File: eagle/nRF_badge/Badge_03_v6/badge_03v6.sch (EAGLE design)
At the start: 43 parts, among them J1 PROG_CONN_6, U1 LIS2DH12, U2 LP2985LV, U3 MCP6231, U5 M95M02, Y1 32768Hz

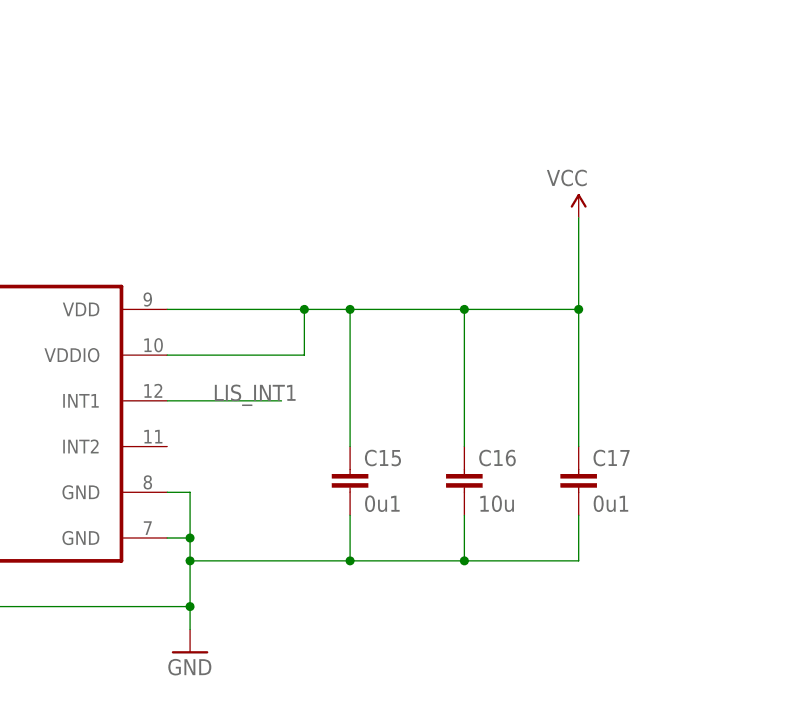
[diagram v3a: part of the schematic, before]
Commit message: Traces cleanup
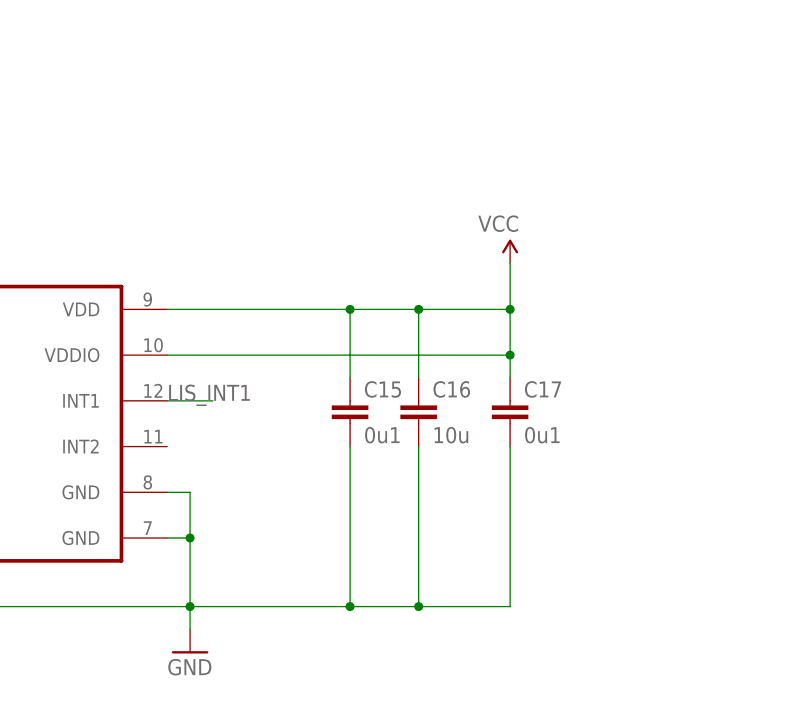
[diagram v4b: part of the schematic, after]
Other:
- moved on the sheet: C15, C16, C17
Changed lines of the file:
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@@
 <instance part="SUPPLY15" gate="G$1" x="12.7" y="43.18" rot="MR0"/>
 <instance part="GND9" gate="1" x="200.66" y="-40.64"/>
-<instance part="C15" gate="G$1" x="218.44" y="-20.32"/>
-<instance part="C16" gate="G$1" x="231.14" y="-20.32"/>
-<instance part="C17" gate="G$1" x="243.84" y="-20.32"/>
-<instance part="SUPPLY18" gate="G$1" x="243.84" y="7.62" rot="MR0"/>
+<instance part="C15" gate="G$1" x="218.44" y="-12.7"/>
+<instance part="C16" gate="G$1" x="226.06" y="-12.7"/>
+<instance part="C17" gate="G$1" x="236.22" y="-12.7"/>
+<instance part="SUPPLY18" gate="G$1" x="236.22" y="2.54" rot="MR0"/>
 <instance part="U1" gate="G$1" x="177.8" y="-15.24"/>
 </instances>
@@
 <wire x1="198.12" y1="-22.86" x2="200.66" y2="-22.86" width="0.1524" layer="91"/>
 <wire x1="200.66" y1="-22.86" x2="200.66" y2="-27.94" width="0.1524" layer="91"/>
-<wire x1="200.66" y1="-27.94" x2="200.66" y2="-30.48" width="0.1524" layer="91"/>
-<wire x1="200.66" y1="-30.48" x2="200.66" y2="-35.56" width="0.1524" layer="91"/>
+<wire x1="200.66" y1="-27.94" x2="200.66" y2="-35.56" width="0.1524" layer="91"/>
 <wire x1="200.66" y1="-35.56" x2="200.66" y2="-38.1" width="0.1524" layer="91"/>
 <wire x1="198.12" y1="-27.94" x2="200.66" y2="-27.94" width="0.1524" layer="91"/>
@@
 <wire x1="157.48" y1="-22.86" x2="154.94" y2="-22.86" width="0.1524" layer="91"/>
 <wire x1="154.94" y1="-22.86" x2="154.94" y2="-27.94" width="0.1524" layer="91"/>
-<pinref part="C17" gate="G$1" pin="2"/>
-<wire x1="243.84" y1="-25.4" x2="243.84" y2="-30.48" width="0.1524" layer="91"/>
-<wire x1="243.84" y1="-30.48" x2="231.14" y2="-30.48" width="0.1524" layer="91"/>
-<pinref part="C16" gate="G$1" pin="2"/>
-<wire x1="231.14" y1="-30.48" x2="218.44" y2="-30.48" width="0.1524" layer="91"/>
-<wire x1="231.14" y1="-25.4" x2="231.14" y2="-30.48" width="0.1524" layer="91"/>
-<junction x="231.14" y="-30.48"/>
-<pinref part="C15" gate="G$1" pin="2"/>
-<wire x1="218.44" y1="-25.4" x2="218.44" y2="-30.48" width="0.1524" layer="91"/>
-<junction x="218.44" y="-30.48"/>
-<wire x1="218.44" y1="-30.48" x2="200.66" y2="-30.48" width="0.1524" layer="91"/>
-<junction x="200.66" y="-30.48"/>
 <pinref part="U1" gate="G$1" pin="RES"/>
 <pinref part="U1" gate="G$1" pin="GND@6"/>
 <pinref part="U1" gate="G$1" pin="GND@7"/>
 <pinref part="U1" gate="G$1" pin="GND@8"/>
+<wire x1="200.66" y1="-35.56" x2="218.44" y2="-35.56" width="0.1524" layer="91"/>
+<pinref part="C17" gate="G$1" pin="2"/>
+<wire x1="218.44" y1="-35.56" x2="226.06" y2="-35.56" width="0.1524" layer="91"/>
+<wire x1="226.06" y1="-35.56" x2="236.22" y2="-35.56" width="0.1524" layer="91"/>
+<wire x1="236.22" y1="-35.56" x2="236.22" y2="-17.78" width="0.1524" layer="91"/>
+<pinref part="C16" gate="G$1" pin="2"/>
+<wire x1="226.06" y1="-17.78" x2="226.06" y2="-35.56" width="0.1524" layer="91"/>
+<junction x="226.06" y="-35.56"/>
+<pinref part="C15" gate="G$1" pin="2"/>
+<wire x1="218.44" y1="-17.78" x2="218.44" y2="-35.56" width="0.1524" layer="91"/>
+<junction x="218.44" y="-35.56"/>
 </segment>
 </net>
@@
 </segment>
 <segment>
-<wire x1="198.12" y1="-7.62" x2="213.36" y2="-7.62" width="0.1524" layer="91"/>
-<wire x1="198.12" y1="-2.54" x2="213.36" y2="-2.54" width="0.1524" layer="91"/>
+<pinref part="SUPPLY18" gate="G$1" pin="VCC"/>
+<pinref part="C17" gate="G$1" pin="1"/>
+<wire x1="236.22" y1="2.54" x2="236.22" y2="-2.54" width="0.1524" layer="91"/>
+<pinref part="U1" gate="G$1" pin="VDDIO"/>
+<wire x1="236.22" y1="-2.54" x2="236.22" y2="-7.62" width="0.1524" layer="91"/>
+<wire x1="236.22" y1="-7.62" x2="236.22" y2="-10.16" width="0.1524" layer="91"/>
+<wire x1="198.12" y1="-7.62" x2="236.22" y2="-7.62" width="0.1524" layer="91"/>
+<junction x="236.22" y="-7.62"/>
+<wire x1="198.12" y1="-2.54" x2="218.44" y2="-2.54" width="0.1524" layer="91"/>
+<pinref part="U1" gate="G$1" pin="VDD"/>
+<wire x1="218.44" y1="-2.54" x2="226.06" y2="-2.54" width="0.1524" layer="91"/>
 <pinref part="C15" gate="G$1" pin="1"/>
-<wire x1="213.36" y1="-2.54" x2="218.44" y2="-2.54" width="0.1524" layer="91"/>
-<wire x1="218.44" y1="-2.54" x2="218.44" y2="-17.78" width="0.1524" layer="91"/>
+<wire x1="218.44" y1="-10.16" x2="218.44" y2="-2.54" width="0.1524" layer="91"/>
+<junction x="218.44" y="-2.54"/>
 <pinref part="C16" gate="G$1" pin="1"/>
-<wire x1="231.14" y1="-17.78" x2="231.14" y2="-2.54" width="0.1524" layer="91"/>
-<wire x1="231.14" y1="-2.54" x2="218.44" y2="-2.54" width="0.1524" layer="91"/>
-<junction x="218.44" y="-2.54"/>
-<wire x1="213.36" y1="-7.62" x2="213.36" y2="-2.54" width="0.1524" layer="91"/>
-<junction x="213.36" y="-2.54"/>
-<wire x1="231.14" y1="-2.54" x2="243.84" y2="-2.54" width="0.1524" layer="91"/>
-<junction x="231.14" y="-2.54"/>
-<pinref part="C17" gate="G$1" pin="1"/>
-<wire x1="243.84" y1="-2.54" x2="243.84" y2="-17.78" width="0.1524" layer="91"/>
-<junction x="243.84" y="-2.54"/>
-<pinref part="SUPPLY18" gate="G$1" pin="VCC"/>
-<wire x1="243.84" y1="7.62" x2="243.84" y2="-2.54" width="0.1524" layer="91"/>
-<pinref part="U1" gate="G$1" pin="VDD"/>
-<pinref part="U1" gate="G$1" pin="VDDIO"/>
+<wire x1="226.06" y1="-10.16" x2="226.06" y2="-2.54" width="0.1524" layer="91"/>
+<junction x="226.06" y="-2.54"/>
+<wire x1="226.06" y1="-2.54" x2="236.22" y2="-2.54" width="0.1524" layer="91"/>
+<junction x="236.22" y="-2.54"/>
 </segment>
 </net>
@@
 <net name="LIS_INT1" class="0">
 <segment>
-<wire x1="198.12" y1="-12.7" x2="210.82" y2="-12.7" width="0.1524" layer="91"/>
+<wire x1="198.12" y1="-12.7" x2="203.2" y2="-12.7" width="0.1524" layer="91"/>
 <pinref part="U1" gate="G$1" pin="INT1"/>
-<label x="203.2" y="-12.7" size="1.778" layer="95"/>
-</segment>
-<segment>
+<label x="198.12" y="-12.7" size="1.778" layer="95"/>
+</segment>
+<segment>

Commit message: change component for comliant design with technical note TN0018
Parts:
- U1: device Badge:LIS2DH12 -> st-microelectronics_modified:LIS2DH12

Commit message: Fix for issues generated in last commit, updated library
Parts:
- U1: value LIS2DH12 -> LIS2DH12"; device st-microelectronics_modified:LIS2DH12 -> Badge:LIS2DH12"
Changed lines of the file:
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@@
 <part name="C17" library="rcl" library_urn="urn:adsk.eagle:library:334" deviceset="C-EU" device="C0603" package3d_urn="urn:adsk.eagle:package:23616/2" value="0u1"/>
 <part name="SUPPLY18" library="Badge" deviceset="VCC" device=""/>
-<part name="U1" library="st-microelectronics_modified" deviceset="LIS2DH12" device=""/>
+<part name="U1" library="Badge" deviceset="LIS2DH12" device="&quot;"/>
 </parts>
 <sheets>

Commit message: Approved Overlap in jumpar pad, errors is cause by DRC but package is fine.
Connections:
- net N$6 renamed ON/OFF
- net N$9 renamed BYPASS
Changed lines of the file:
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@@
 <part name="C4" library="rcl" library_urn="urn:adsk.eagle:library:334" deviceset="C-EU" device="C0603" package3d_urn="urn:adsk.eagle:package:23616/2" value="12p"/>
 <part name="GND10" library="Badge" deviceset="GND" device=""/>
-<part name="M_ENA" library="Badge" deviceset="JUMPER-PAD-3-2OF3_NC_BY_TRACE" device="_SMALL" value=""/>
+<part name="M_ENA" library="Badge" deviceset="JUMPER-PAD-3-2OF3_NC_BY_TRACE" device="_SMALL" value="JUMPER-PAD-3-2OF3_NC_BY_TRACE_SMALL"/>
 <part name="SUPPLY9" library="Badge" deviceset="VCC" device=""/>
 <part name="A1" library="rigado_BMD-200" deviceset="BMD-200" device=""/>
@@
 </segment>
 </net>
-<net name="N$6" class="0">
+<net name="ON/OFF" class="0">
 <segment>
 <pinref part="U2" gate="G$1" pin="ON/OFF"/>
@@
 </segment>
 </net>
-<net name="N$9" class="0">
+<net name="BYPASS" class="0">
 <segment>
 <pinref part="U2" gate="G$1" pin="BYPASS"/>
